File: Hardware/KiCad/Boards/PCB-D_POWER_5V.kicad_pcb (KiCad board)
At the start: 2 copper layers, 125 x 94 mm, 0 parts

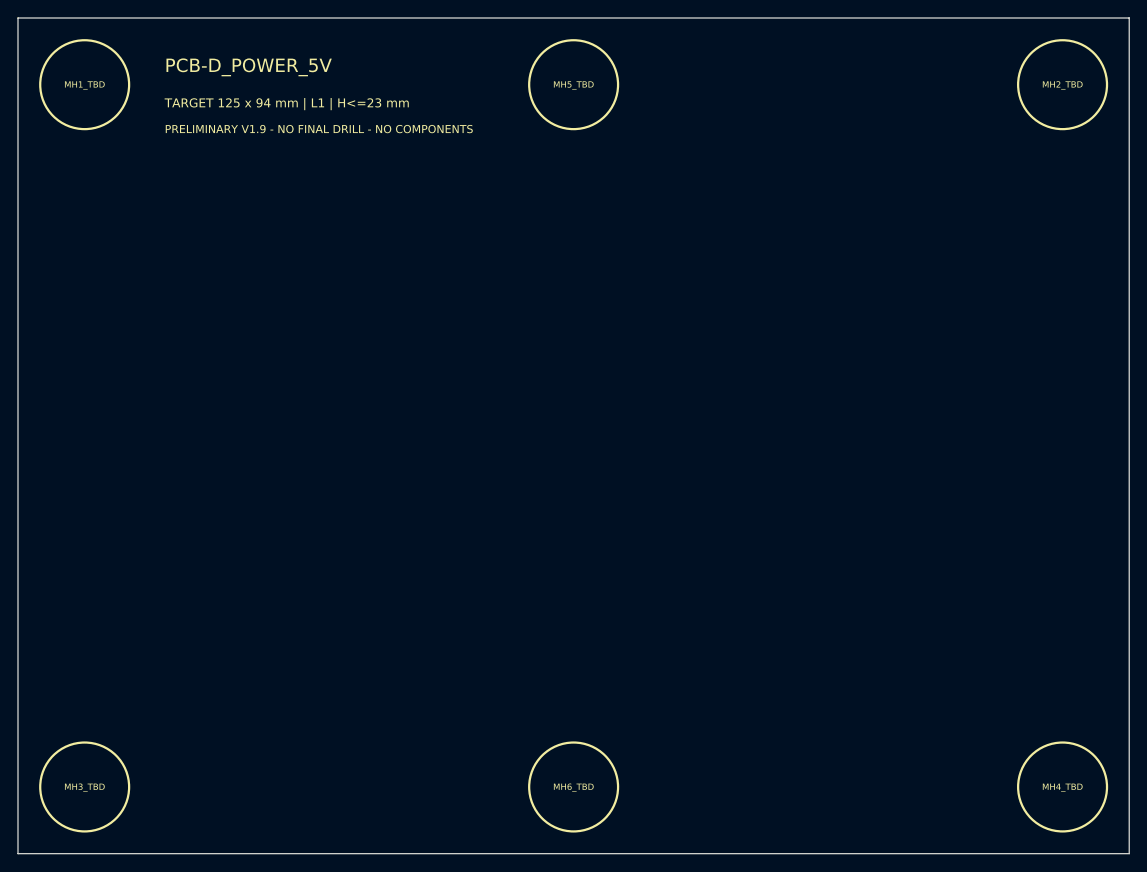
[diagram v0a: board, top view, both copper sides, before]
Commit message: hardware: add PCB-D functional, height and thermal placeholders
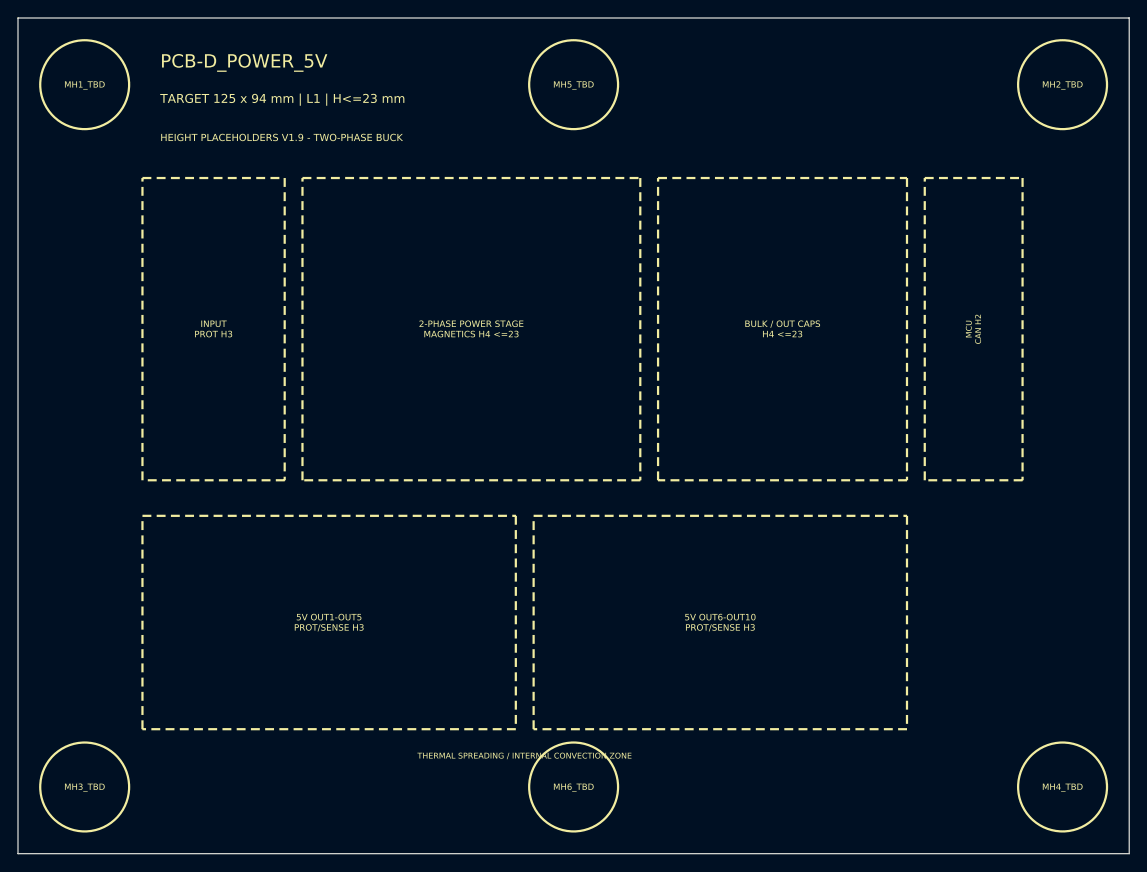
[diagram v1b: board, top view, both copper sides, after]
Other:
- board text added: "2-PHASE POWER STAGE MAGNETICS H4 <=23"
- board text added: "5V OUT1-OUT5 PROT/SENSE H3"
- board text added: "5V OUT6-OUT10 PROT/SENSE H3"
- board text added: "BULK / OUT CAPS H4 <=23"
- board text added: "HEIGHT PLACEHOLDERS V1.9 - TWO-PHASE BUCK"
- board text added: "INPUT PROT H3"
- board text added: "MCU CAN H2"
- board text added: "THERMAL SPREADING / INTERNAL CONVECTION ZONE"
- board text removed: "PRELIMINARY V1.9 - NO FINAL DRILL - NO COMPONENTS"
